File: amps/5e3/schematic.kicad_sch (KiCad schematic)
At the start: 44 parts, among them T2 8k:8

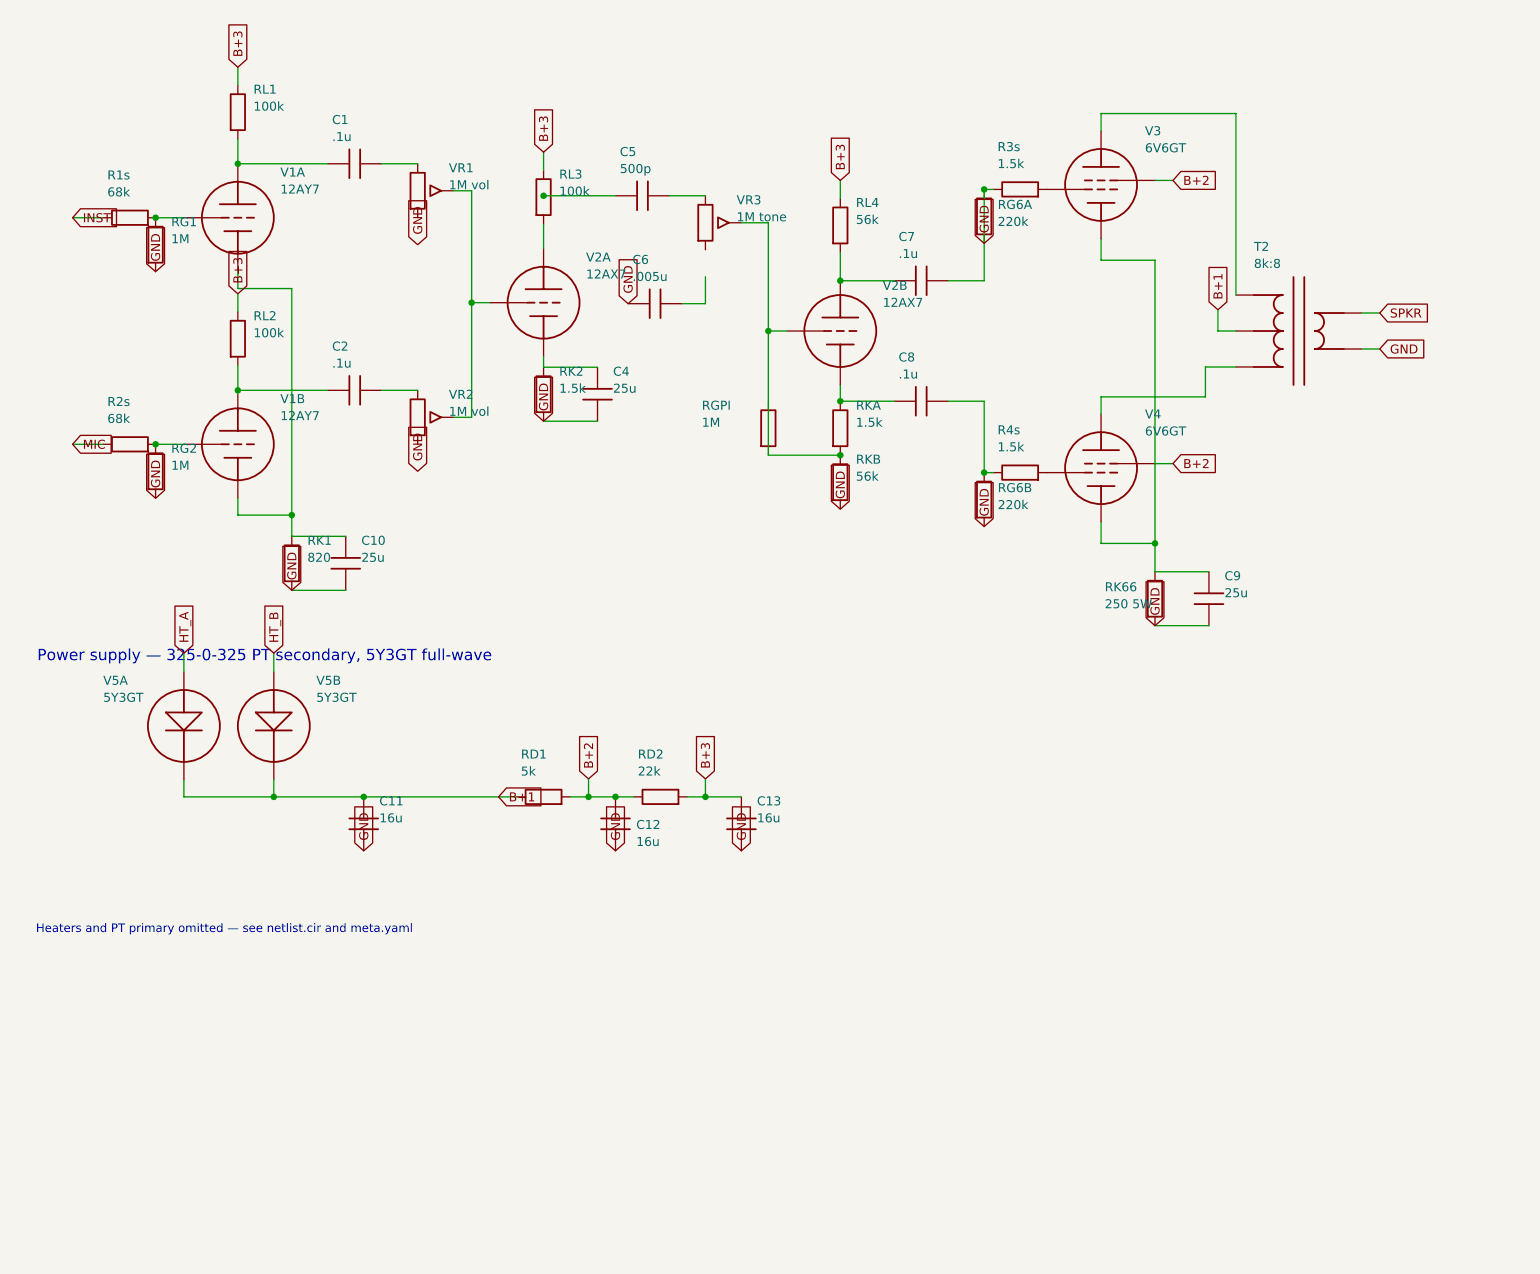
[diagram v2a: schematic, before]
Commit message: Fix: rotated global labels lettered their net names outside the flag
Every global label this pipeline emitted carried (justify left) regardless of
rotation. KiCanvas — like KiCad — draws label text horizontally at 0/180 and
vertically at 90/270 and reads WHICH SIDE of the anchor it letters on from the
justification, so at 180 and 270 the name printed outside an empty flag
outline, struck through by the very wire it names: 219 labels at 180 deg
(including the input-jack flags at top-left of nearly every sheet, the first
glyphs a visitor reads) and 792 GND/rail flags at 270 whose names squeezed at
the flag mouth instead of lettering down the body. The library already
compensated rotation for property text (`pa`); this mirrors that logic for
global labels: justify right at 180/270, left at 0/90.

check_schematics gains the geometry clause whose absence let all 1011
instances through a "no lettering through circuitry" pass: it modelled the
flag box but never the label TEXT, so a name rendered on the wrong side was
invisible to it. The gate now proves justification compensates rotation on
every global label.

Two more things this exposed, fixed in the same engine pass:

- Placement now measures with the renderer's own Newstroke advance table
  (extracted from the vendored kicanvas.js) instead of a flat 0.68-em prose
  average that under-read part lettering by a quarter — the mechanism behind
  every "metered clean, printed through its neighbour" incident. The GATE
  deliberately keeps the coarse ruler: re-ruling it with renderer truth was
  tried and red-flagged 28 of 34 sheets over abutments three visual passes
  had already judged sub-visual (the two-rulers note in schematic_lib.py).
- place_captions' escape ladder runs further, because a banner caption
  measured truly is half again wider than the old estimate believed.

All 34 schematics regenerated; full gate suite green.

🤖 Generated with [Claude Code](https://claude.com/claude-code)

Co-Authored-By: Claude Fable 5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
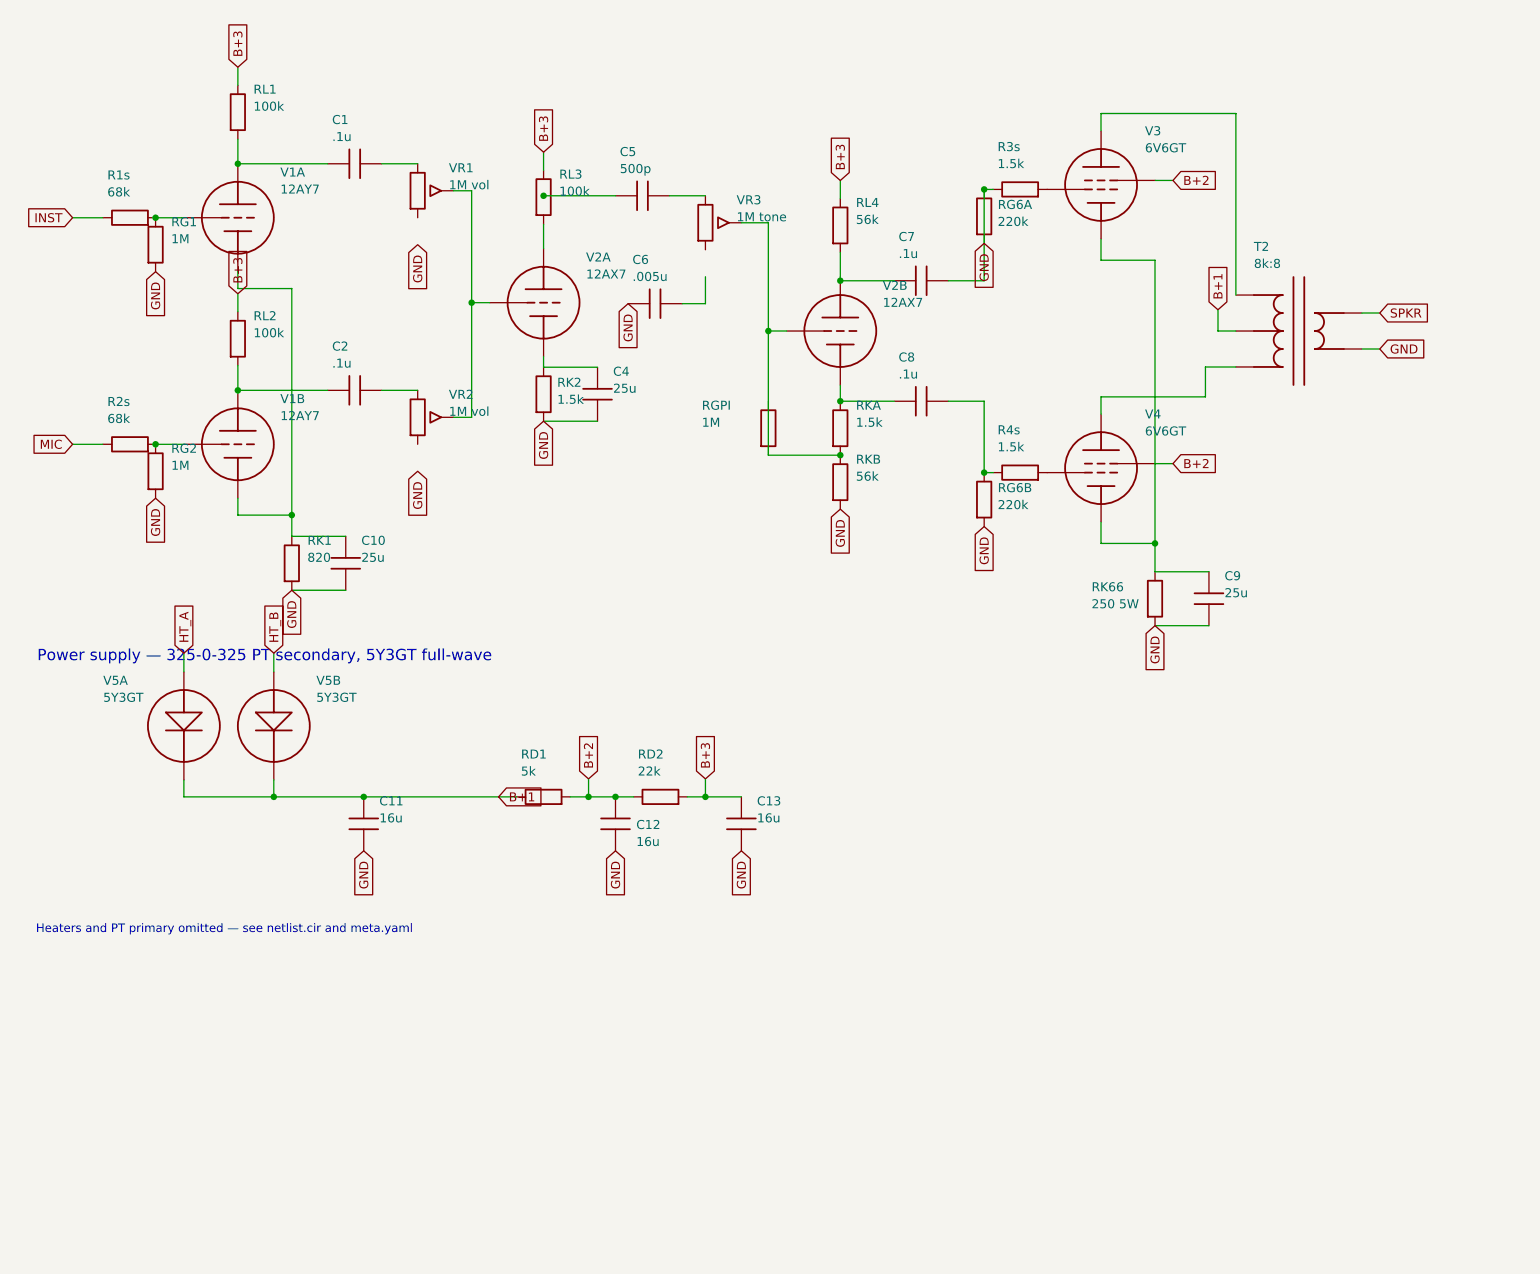
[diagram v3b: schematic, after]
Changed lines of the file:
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@@
     (comment 3 "Values read from: https://el34world.com/charts/Schematics/files/Fender/Fender_deluxe_5e3.pdf"))
   (global_label "INST" (shape input) (at 17.8816 38.278 180)
-    (effects (font (size 1.27 1.27)) (justify left)))
+    (effects (font (size 1.27 1.27)) (justify right)))
   (wire (pts (xy 17.8816 38.278) (xy 22.1716 38.278))
     (stroke (width 0) (type default)))
@@
     (stroke (width 0) (type default)))
   (global_label "GND" (shape input) (at 29.6016 45.898 270)
-    (effects (font (size 1.27 1.27)) (justify left)))
+    (effects (font (size 1.27 1.27)) (justify right)))
   (wire (pts (xy 41.2216 30.658) (xy 41.2216 27.178))
     (stroke (width 0) (type default)))
@@
     (effects (font (size 1.27 1.27)) (justify left)))
   (global_label "MIC" (shape input) (at 17.8816 70.278 180)
-    (effects (font (size 1.27 1.27)) (justify left)))
+    (effects (font (size 1.27 1.27)) (justify right)))
   (wire (pts (xy 17.8816 70.278) (xy 22.1716 70.278))
     (stroke (width 0) (type default)))
@@
     (stroke (width 0) (type default)))
   (global_label "GND" (shape input) (at 29.6016 77.898 270)
-    (effects (font (size 1.27 1.27)) (justify left)))
+    (effects (font (size 1.27 1.27)) (justify right)))
   (wire (pts (xy 41.2216 62.658) (xy 41.2216 59.178))
     (stroke (width 0) (type default)))
@@
     (stroke (width 0) (type default)))
   (global_label "GND" (shape input) (at 48.8416 90.898 270)
-    (effects (font (size 1.27 1.27)) (justify left)))
+    (effects (font (size 1.27 1.27)) (justify right)))
   (wire (pts (xy 41.2216 30.658) (xy 53.9216 30.658))
     (stroke (width 0) (type default)))
@@
     (property "Value" "1M vol" (at 71.0216 33.668 0) (effects (font (size 1.27 1.27)) (justify left))))
   (global_label "GND" (shape input) (at 66.6216 42.088 270)
-    (effects (font (size 1.27 1.27)) (justify left)))
+    (effects (font (size 1.27 1.27)) (justify right)))
   (wire (pts (xy 71.7016 34.468) (xy 74.2416 34.468))
     (stroke (width 0) (type default)))
@@
     (property "Value" "1M vol" (at 71.0216 65.668 0) (effects (font (size 1.27 1.27)) (justify left))))
   (global_label "GND" (shape input) (at 66.6216 74.088 270)
-    (effects (font (size 1.27 1.27)) (justify left)))
+    (effects (font (size 1.27 1.27)) (justify right)))
   (wire (pts (xy 71.7016 66.468) (xy 74.2416 66.468))
     (stroke (width 0) (type default)))
@@
   (symbol (lib_id "cx:R") (at 84.4016 63.208 0) (unit 1)
     (in_bom yes) (on_board yes)
-    (property "Reference" "RK2" (at 86.6016 60.008 0) (effects (font (size 1.27 1.27)) (justify left)))
-    (property "Value" "1.5k" (at 86.6016 62.408 0) (effects (font (size 1.27 1.27)) (justify left))))
+    (property "Reference" "RK2" (at 86.3176 61.568 0) (effects (font (size 1.27 1.27)) (justify left)))
+    (property "Value" "1.5k" (at 86.3176 63.968 0) (effects (font (size 1.27 1.27)) (justify left))))
   (symbol (lib_id "cx:C") (at 92.0216 63.208 0) (unit 1)
     (in_bom yes) (on_board yes)
@@
     (stroke (width 0) (type default)))
   (global_label "GND" (shape input) (at 84.4016 67.018 270)
-    (effects (font (size 1.27 1.27)) (justify left)))
+    (effects (font (size 1.27 1.27)) (justify right)))
   (wire (pts (xy 84.4016 57.898) (xy 84.4016 59.398))
     (stroke (width 0) (type default)))
@@
     (stroke (width 0) (type default)))
   (global_label "GND" (shape input) (at 96.3416 50.418 270)
-    (effects (font (size 1.27 1.27)) (justify left)))
+    (effects (font (size 1.27 1.27)) (justify right)))
   (wire (pts (xy 112.342 38.988) (xy 116.152 38.988))
     (stroke (width 0) (type default)))
@@
     (property "Value" "56k" (at 128.512 74.828 0) (effects (font (size 1.27 1.27)) (justify left))))
   (global_label "GND" (shape input) (at 126.312 79.438 270)
-    (effects (font (size 1.27 1.27)) (justify left)))
+    (effects (font (size 1.27 1.27)) (justify right)))
   (wire (pts (xy 116.152 54.278) (xy 116.152 71.818))
     (stroke (width 0) (type default)))
@@
     (property "Value" "220k" (at 148.548 38.848 0) (effects (font (size 1.27 1.27)) (justify left))))
   (global_label "GND" (shape input) (at 146.632 41.898 270)
-    (effects (font (size 1.27 1.27)) (justify left)))
+    (effects (font (size 1.27 1.27)) (justify right)))
   (wire (pts (xy 170.762 33.008) (xy 173.302 33.008))
     (stroke (width 0) (type default)))
@@
     (property "Value" "220k" (at 148.548 78.848 0) (effects (font (size 1.27 1.27)) (justify left))))
   (global_label "GND" (shape input) (at 146.632 81.898 270)
-    (effects (font (size 1.27 1.27)) (justify left)))
+    (effects (font (size 1.27 1.27)) (justify right)))
   (wire (pts (xy 170.762 73.008) (xy 173.302 73.008))
     (stroke (width 0) (type default)))
@@
   (symbol (lib_id "cx:R") (at 170.762 92.088 0) (unit 1)
     (in_bom yes) (on_board yes)
-    (property "Reference" "RK66" (at 163.664 90.448 0) (effects (font (size 1.27 1.27)) (justify left)))
-    (property "Value" "250 5W" (at 163.664 92.848 0) (effects (font (size 1.27 1.27)) (justify left))))
+    (property "Reference" "RK66" (at 161.796 90.448 0) (effects (font (size 1.27 1.27)) (justify left)))
+    (property "Value" "250 5W" (at 161.796 92.848 0) (effects (font (size 1.27 1.27)) (justify left))))
   (symbol (lib_id "cx:C") (at 178.382 92.088 0) (unit 1)
     (in_bom yes) (on_board yes)
@@
     (stroke (width 0) (type default)))
   (global_label "GND" (shape input) (at 170.762 95.898 270)
-    (effects (font (size 1.27 1.27)) (justify left)))
+    (effects (font (size 1.27 1.27)) (justify right)))
   (symbol (lib_id "cx:OT_PP") (at 191.082 54.278 0) (unit 1)
     (in_bom yes) (on_board yes)
@@
     (property "Value" "16u" (at 61.2016 123.088 0) (effects (font (size 1.27 1.27)) (justify left))))
   (global_label "GND" (shape input) (at 59.0016 127.698 270)
-    (effects (font (size 1.27 1.27)) (justify left)))
+    (effects (font (size 1.27 1.27)) (justify right)))
   (global_label "B+1" (shape input) (at 78.0516 120.078 0)
     (effects (font (size 1.27 1.27)) (justify left)))
@@
     (property "Value" "16u" (at 97.4936 126.426 0) (effects (font (size 1.27 1.27)) (justify left))))
   (global_label "GND" (shape input) (at 94.5616 127.698 270)
-    (effects (font (size 1.27 1.27)) (justify left)))
+    (effects (font (size 1.27 1.27)) (justify right)))
   (symbol (lib_id "cx:R") (at 100.912 120.078 90) (unit 1)
     (in_bom yes) (on_board yes)
@@
     (property "Value" "16u" (at 114.542 123.088 0) (effects (font (size 1.27 1.27)) (justify left))))
   (global_label "GND" (shape input) (at 112.342 127.698 270)
-    (effects (font (size 1.27 1.27)) (justify left)))
+    (effects (font (size 1.27 1.27)) (justify right)))
   (text "Heaters and PT primary omitted — see netlist.cir and meta.yaml" (at 12.7 138.856 0)
     (effects (font (size 1.2 1.2)) (justify left)))
